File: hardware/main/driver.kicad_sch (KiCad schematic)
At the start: 12 parts, among them U501 1EDI60N12AF

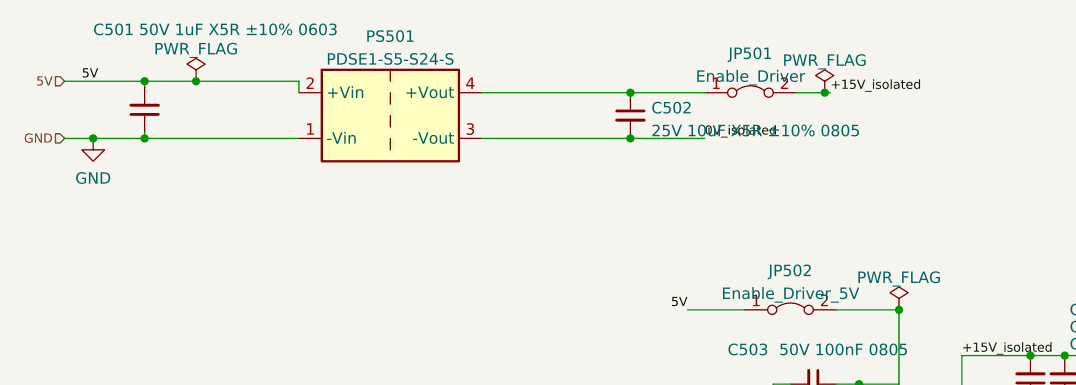
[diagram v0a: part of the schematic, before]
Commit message: Layout: Place components and route analog, supplies and CAN
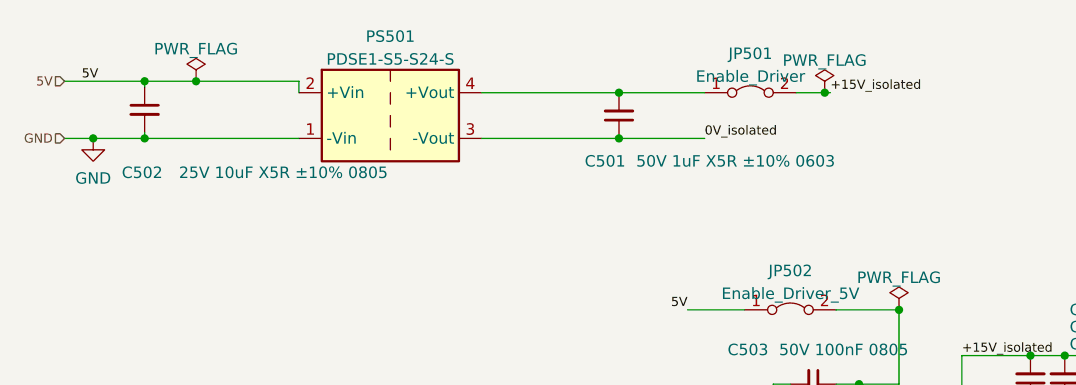
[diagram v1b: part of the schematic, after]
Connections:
- net 5V: now also C502.1; no longer C501.2
- net GND: now also C502.2; no longer C501.1
- net OUT_S: now also C501.1; no longer C502.2
- net at JP501.1 (A), PS501.4 (+Vout): now also C501.2; no longer C502.1
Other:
- moved on the sheet: C501, C502
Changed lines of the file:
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@@
   (junction (at 125.095 65.405) (diameter 0) (color 0 0 0 0)
   )
-  (junction (at 103.505 65.405) (diameter 0) (color 0 0 0 0)
+  (junction (at 102.235 70.485) (diameter 0) (color 0 0 0 0)
   )
   (junction (at 128.905 97.79) (diameter 0) (color 0 0 0 0)
   )
-  (junction (at 103.505 70.485) (diameter 0) (color 0 0 0 0)
+  (junction (at 102.235 65.405) (diameter 0) (color 0 0 0 0)
   )
   (junction (at 133.35 89.535) (diameter 0) (color 0 0 0 0)
@@
     (stroke (width 0) (type default) (color 0 0 0 0))
   )
+  (wire (pts (xy 102.235 65.405) (xy 111.76 65.405))
+    (stroke (width 0) (type default) (color 0 0 0 0))
+  )
   (wire (pts (xy 105.41 110.49) (xy 122.555 110.49))
     (stroke (width 0) (type default) (color 0 0 0 0))
@@
     (stroke (width 0) (type default) (color 0 0 0 0))
   )
-  (wire (pts (xy 103.505 65.405) (xy 111.76 65.405))
-    (stroke (width 0) (type default) (color 0 0 0 0))
-  )
   (wire (pts (xy 116.84 117.475) (xy 116.84 115.57))
     (stroke (width 0) (type default) (color 0 0 0 0))
   )
-  (wire (pts (xy 86.995 70.485) (xy 103.505 70.485))
+  (wire (pts (xy 86.995 70.485) (xy 102.235 70.485))
     (stroke (width 0) (type default) (color 0 0 0 0))
   )
@@
     (stroke (width 0) (type default) (color 0 0 0 0))
   )
+  (wire (pts (xy 102.235 70.485) (xy 111.76 70.485))
+    (stroke (width 0) (type default) (color 0 0 0 0))
+  )
   (wire (pts (xy 133.35 89.535) (xy 133.35 97.79))
     (stroke (width 0) (type default) (color 0 0 0 0))
   )
-  (wire (pts (xy 86.995 65.405) (xy 103.505 65.405))
+  (wire (pts (xy 86.995 65.405) (xy 102.235 65.405))
     (stroke (width 0) (type default) (color 0 0 0 0))
   )
@@
   )
   (wire (pts (xy 126.365 89.535) (xy 133.35 89.535))
-    (stroke (width 0) (type default) (color 0 0 0 0))
-  )
-  (wire (pts (xy 103.505 70.485) (xy 111.76 70.485))
     (stroke (width 0) (type default) (color 0 0 0 0))
   )
@@
     (pin "1")
   )
-  (symbol (lib_id "Device:C_Small") (at 49.53 67.31 0) (mirror x) (unit 1)
+  (symbol (lib_id "Device:C_Small") (at 102.235 67.945 0) (mirror x) (unit 1)
     (in_bom yes) (on_board yes)
-    (property "Reference" "C501" (id 0) (at 43.815 58.42 0)
-      (effects (font (size 1.27 1.27)) (justify left))
-    )
-    (property "Value" "50V 1uF X5R ±10% 0603" (id 1) (at 48.895 58.42 0)
-      (effects (font (size 1.27 1.27)) (justify left))
-    )
-    (property "Footprint" "Capacitor_SMD:C_0603_1608Metric_Pad1.08x0.95mm_HandSolder" (id 2) (at 49.53 67.31 0)
-      (effects (font (size 1.27 1.27)) hide)
-    )
-    (property "Datasheet" "~" (id 3) (at 49.53 67.31 0)
+    (property "Reference" "C501" (id 0) (at 98.425 73.025 0)
+      (effects (font (size 1.27 1.27)) (justify left))
+    )
+    (property "Value" "50V 1uF X5R ±10% 0603" (id 1) (at 104.14 73.025 0)
+      (effects (font (size 1.27 1.27)) (justify left))
+    )
+    (property "Footprint" "Capacitor_SMD:C_0603_1608Metric_Pad1.08x0.95mm_HandSolder" (id 2) (at 102.235 67.945 0)
+      (effects (font (size 1.27 1.27)) hide)
+    )
+    (property "Datasheet" "~" (id 3) (at 102.235 67.945 0)
       (effects (font (size 1.27 1.27)) hide)
     )
@@
     (pin "2")
   )
-  (symbol (lib_id "Device:C_Small") (at 103.505 67.945 0) (unit 1)
-    (in_bom yes) (on_board yes) (fields_autoplaced)
-    (property "Reference" "C502" (id 0) (at 105.8291 67.1166 0)
-      (effects (font (size 1.27 1.27)) (justify left))
-    )
-    (property "Value" "25V 10uF X5R ±10% 0805" (id 1) (at 105.8291 69.6535 0)
-      (effects (font (size 1.27 1.27)) (justify left))
-    )
-    (property "Footprint" "Capacitor_SMD:C_0805_2012Metric_Pad1.18x1.45mm_HandSolder" (id 2) (at 103.505 67.945 0)
-      (effects (font (size 1.27 1.27)) hide)
-    )
-    (property "Datasheet" "~" (id 3) (at 103.505 67.945 0)
-      (effects (font (size 1.27 1.27)) hide)
-    )
+  (symbol (lib_id "Device:C_Small") (at 49.53 67.31 0) (unit 1)
+    (in_bom yes) (on_board yes)
+    (property "Reference" "C502" (id 0) (at 46.99 74.295 0)
+      (effects (font (size 1.27 1.27)) (justify left))
+    )
+    (property "Value" "25V 10uF X5R ±10% 0805" (id 1) (at 53.34 74.295 0)
+      (effects (font (size 1.27 1.27)) (justify left))
+    )
+    (property "Footprint" "Capacitor_SMD:C_0805_2012Metric_Pad1.18x1.45mm_HandSolder" (id 2) (at 49.53 67.31 0)
+      (effects (font (size 1.27 1.27)) hide)
+    )
+    (property "Datasheet" "~" (id 3) (at 49.53 67.31 0)
+      (effects (font (size 1.27 1.27)) hide)
+    )
